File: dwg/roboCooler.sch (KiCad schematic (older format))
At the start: 36 parts, among them J1 CONN_02X25, J10 CONN_01X12, J11 CONN_01X12, J12 CONN_01X04, J13 CONN_01X04, J14 CONN_01X04, J15 CONN_01X04, J2 CONN_02X25, J3 CONN_01X04, J4 CONN_01X02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

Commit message: fixed connector 3d view on board.
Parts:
- J1, J2: footprint Socket_Strips:Socket_Strip_Straight_2x25 -> roboCooler:Socket_Strip_Straight_2x25_Inverted
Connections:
- net hBridge/SIGNAL GND is gone; now on net hBridge/SIGNAL GND: J15.4 (P4)
- net hBridge/SIGNAL GND: no longer J13.2 (P2)
- new net hBridge/SIGNAL GND: J13.2 (P2)
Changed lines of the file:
@@
 F 0 "J1" H 1450 3300 50  0000 C CNN
 F 1 "CONN_02X25" V 1450 2000 50  0000 C CNN
-F 2 "Socket_Strips:Socket_Strip_Straight_2x25" H 1450 1250 60  0001 C CNN
+F 2 "roboCooler:Socket_Strip_Straight_2x25_Inverted" H 1450 1250 60  0001 C CNN
 F 3 "" H 1450 1250 60  0000 C CNN
 	1    1450 2000
@@
 F 0 "J2" H 3400 3300 50  0000 C CNN
 F 1 "CONN_02X25" V 3400 2000 50  0000 C CNN
-F 2 "Socket_Strips:Socket_Strip_Straight_2x25" H 3400 1250 60  0001 C CNN
+F 2 "roboCooler:Socket_Strip_Straight_2x25_Inverted" H 3400 1250 60  0001 C CNN
 F 3 "" H 3400 1250 60  0000 C CNN
 	1    3400 2000

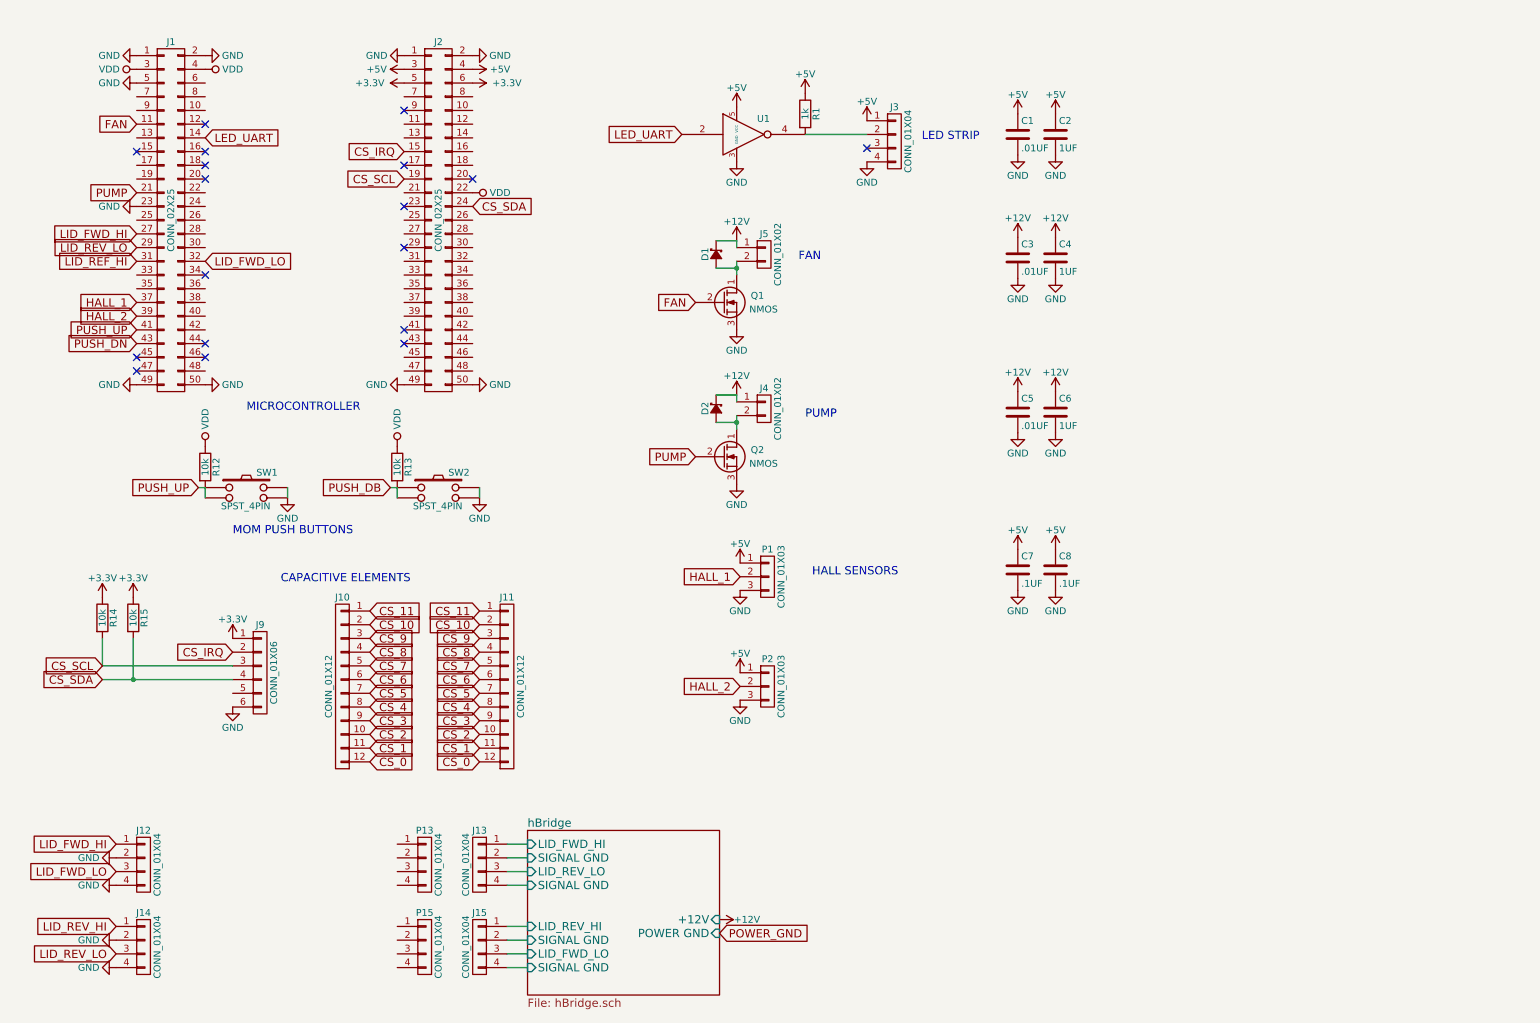
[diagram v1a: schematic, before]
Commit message: added motor driver chip to schematic and removed hbridge
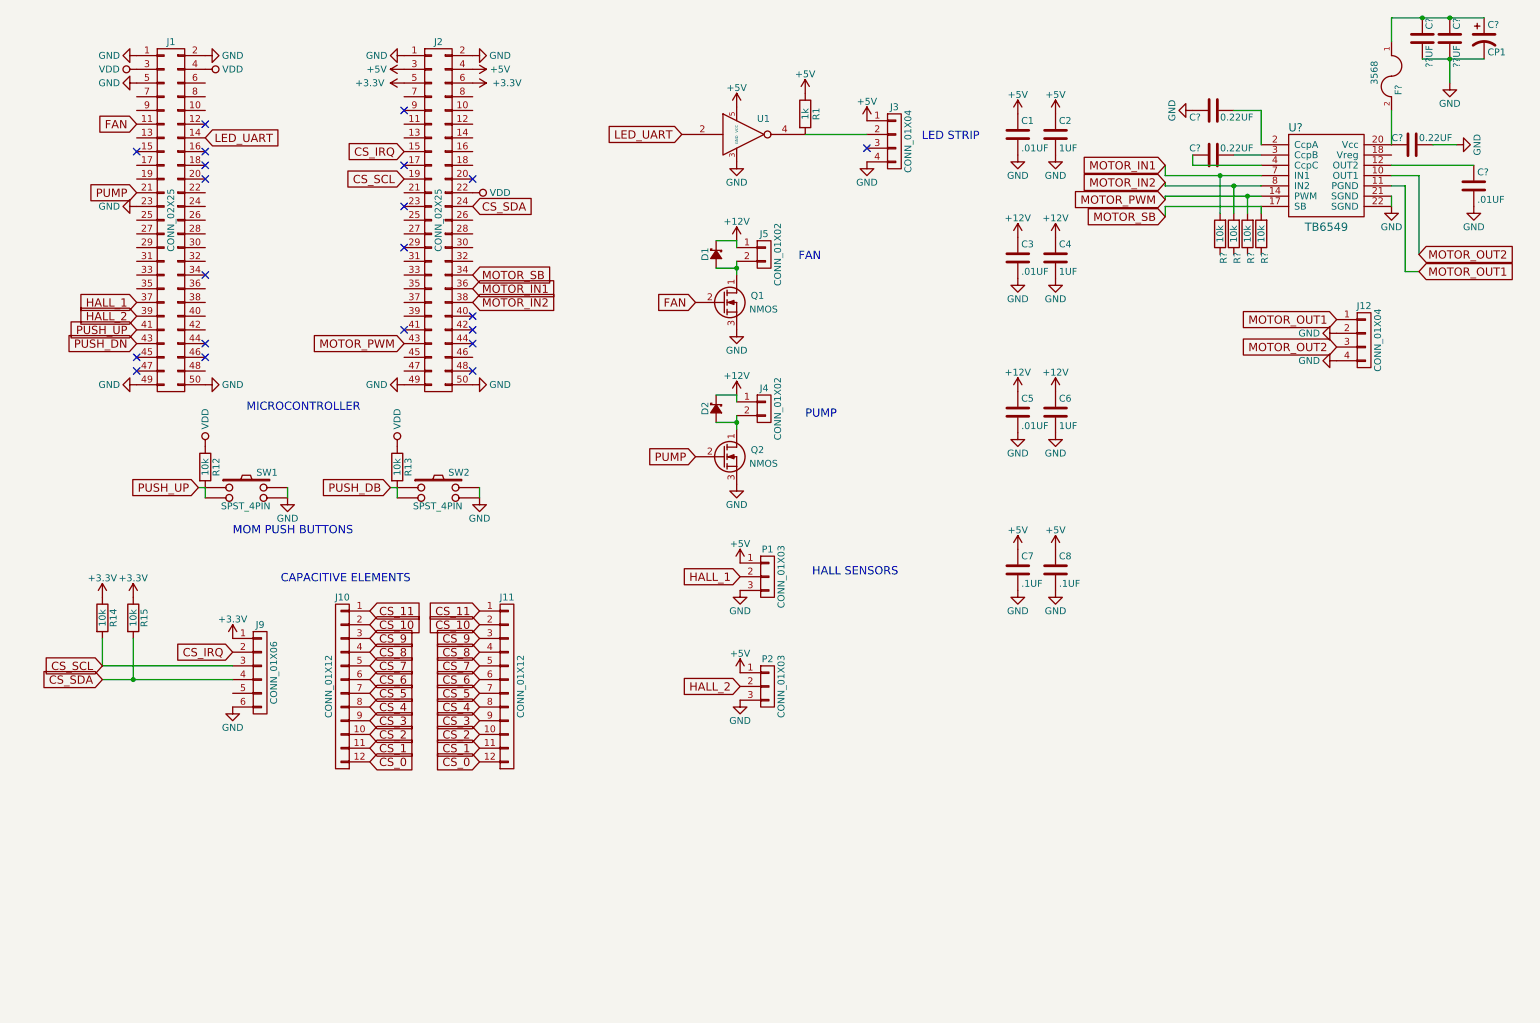
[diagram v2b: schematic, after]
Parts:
- removed J13, J14, J15, P13, P15: CONN_01X04, symbol CONN_01X04
- added C? (x3): 0.22UF, Capacitors_SMD:C_0805_HandSoldering, symbol C
- added C?: .01UF, Capacitors_SMD:C_0805_HandSoldering, symbol C
- added C? (x2): ??UF, Capacitors_SMD:C_0805_HandSoldering, symbol C
- added C?: CP1, symbol CP1
- added F?: 3568, symbol FUSE
- added R? (x4): 10k, Resistors_SMD:R_0805_HandSoldering, symbol R
- added U?: TB6549, symbol TB6549
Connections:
- net GND: now also C?.1, C?.1, C?.1, C?.2, C?.2, C?.2, U?.21 (SGND), U?.22 (SGND)
- net MOTOR_SB: now reaches J2.34 (P34)
- net MOTOR_SB: now also R?.2, U?.17 (SB)
- net MOTOR_IN1: now reaches J2.36 (P36)
- net MOTOR_IN1: now also R?.2, U?.7 (IN1)
- net MOTOR_IN2: now reaches J2.38 (P38)
- net MOTOR_IN2: now also R?.2, U?.8 (IN2)
- net MOTOR_PWM: now reaches J2.43 (P43)
- net MOTOR_PWM: now also R?.2, U?.14 (PWM)
- net LID_FWD_HI: no longer names the net of J1.27 (P27)
- net LID_FWD_HI: no longer J12.1 (P1)
- net LID_FWD_LO: no longer names the net of J1.32 (P32)
- net LID_FWD_LO: no longer J12.3 (P3)
- net LID_REF_HI: no longer names the net of J1.31 (P31)
- net LID_REV_LO: no longer names the net of J1.29 (P29)
- new net: C?.1, U?.12 (OUT2)
- new net: C?.1, U?.2 (CcpA)
- new net: C?.2, F?.2, U?.20 (Vcc)
- new net: C?.1, U?.3 (CcpB)
- new net: C?.2, U?.4 (CcpC)
- new net: C?.1, C?.2, C?.2, F?.1
- new net MOTOR_OUT1: J12.1 (P1), U?.11 (PGND)
- new net MOTOR_OUT2: J12.3 (P3), U?.10 (OUT1)
- no-connect marks 18 -> 21
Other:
- moved on the sheet: J12

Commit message: placed components for motor driver
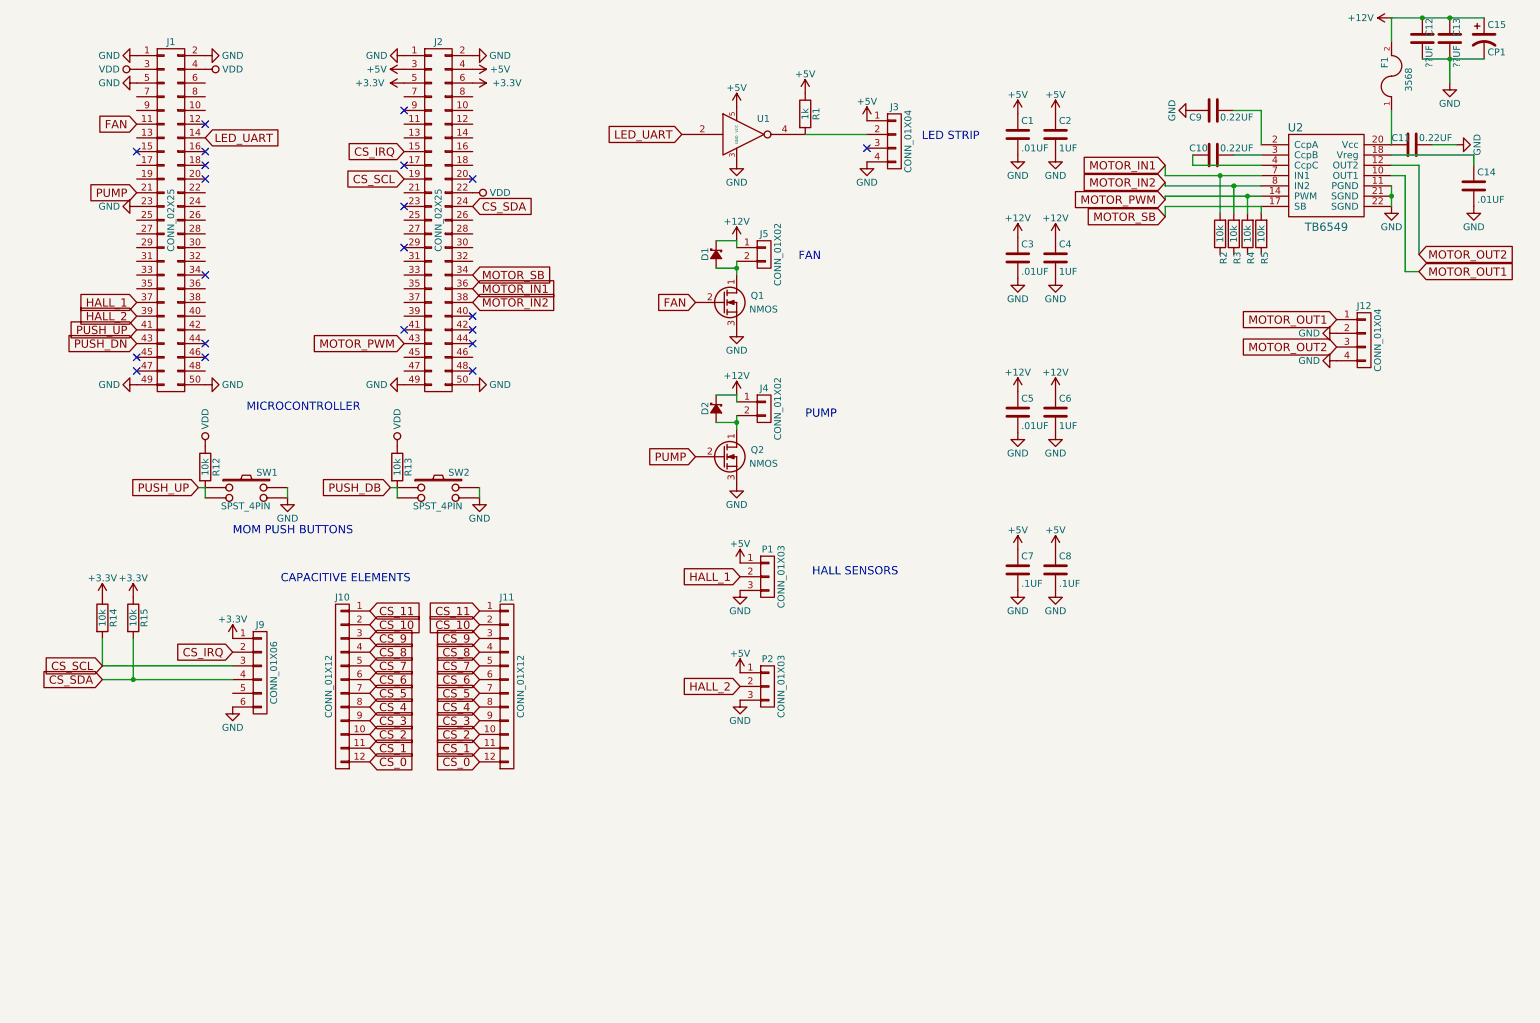
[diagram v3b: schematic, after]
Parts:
- F1: renamed from F?; footprint (none) -> roboCooler:3568
- U2: renamed from U?; footprint (none) -> roboCooler:TB6549
- gave numbers to parts that had none: 11
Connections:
- net +12V: now also C12.2, C13.2, C15.1, F1.2
- net GND: now also U2.11 (PGND)
- net MOTOR_OUT1: now also U2.10 (OUT1); no longer U2.11 (PGND)
- net MOTOR_OUT2: now also U2.12 (OUT2); no longer U2.10 (OUT1)
- net at C14.1: now also U2.18 (Vreg); no longer U2.12 (OUT2)
- net at C11.2, U2.20 (Vcc): now also F1.1; no longer F1.2

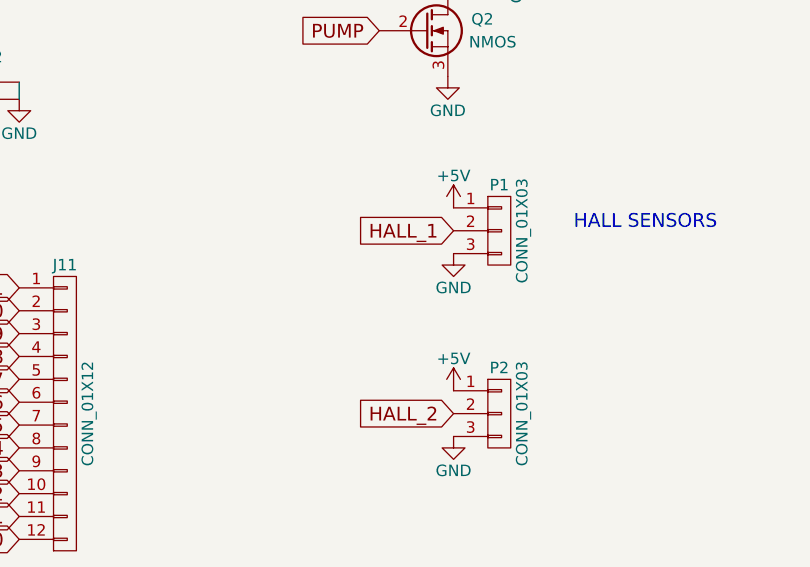
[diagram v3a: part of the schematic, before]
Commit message: added pull up resistors to hall effect sensors
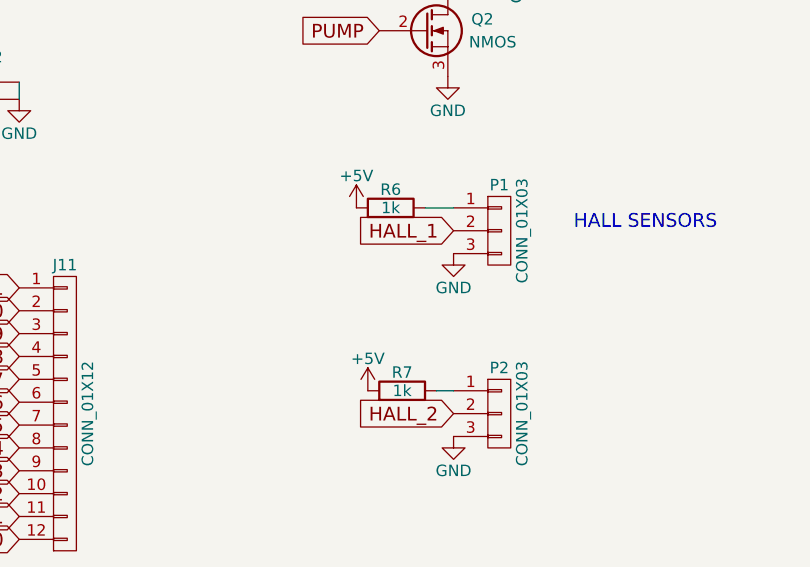
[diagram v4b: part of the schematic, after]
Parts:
- added R6, R7: 1k, Resistors_SMD:R_0805_HandSoldering, symbol R
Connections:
- net +5V: now also R6.2, R7.2; no longer P1.1 (P1), P2.1 (P1)
- new net: P1.1 (P1), R6.1
- new net: P2.1 (P1), R7.1
